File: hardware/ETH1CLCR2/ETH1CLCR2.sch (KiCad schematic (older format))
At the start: 0 parts

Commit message: PCB
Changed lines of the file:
@@
 F13 "TRIG_OUT" O R 8400 1600 50
 F14 "TRIG_IN" I R 8400 1700 50
-F15 "SPI2_MOSI" O L 6900 3750 50
-F16 "SPI2_NSS" O L 6900 3650 50
-F17 "SPI2_SCK" O L 6900 3850 50
-F18 "SPI1_NSS" O L 6900 4100 50
-F19 "SPI1_SCK" O L 6900 4200 50
-F20 "SPI1_MOSI" O L 6900 4300 50
-F21 "SPI3_MOSI" O L 6900 1900 50
-F22 "SPI3_MISO" I L 6900 2000 50
-F23 "SPI3_SCK" O L 6900 1800 50
-F24 "SPI3_NSS" O L 6900 1700 50
-F25 "CXN_REL5" O R 8400 3800 50
-F26 "CXN_REL4" O R 8400 3700 50
-F27 "CXN_REL3" O R 8400 3600 50
-F28 "CXN_REL2" O R 8400 3500 50
-F29 "CXN_REL1" O R 8400 3400 50
-F30 "IRR1" O L 6900 5900 50
-F31 "IRR2" O L 6900 6000 50
-F32 "IRR3" O L 6900 6100 50
-F33 "IRR4" O L 6900 6200 50
-F34 "IRR0" O L 6900 5800 50
-F35 "VDIFF2" O L 6900 5500 50
-F36 "VDIFF1" O L 6900 5400 50
-F37 "VDIFF0" O L 6900 5300 50
-F38 "IDIFF1" O L 6900 5700 50
-F39 "IDIFF0" O L 6900 5600 50
-F40 "SPI1_MISO" I L 6900 4000 50
-F41 "ADC1_RVS1" I L 6900 1500 50
-F42 "ADC1_RVS2" I L 6900 1600 50
+F15 "SPI2_NSS" O L 6900 2300 50
+F16 "SPI2_SCK" O L 6900 2400 50
+F17 "SPI1_NSS" O L 6900 4100 50
+F18 "SPI1_SCK" O L 6900 4200 50
+F19 "SPI1_MOSI" O L 6900 4300 50
+F20 "SPI3_MOSI" O L 6900 1900 50
+F21 "SPI3_MISO" I L 6900 2000 50
+F22 "SPI3_SCK" O L 6900 1800 50
+F23 "SPI3_NSS" O L 6900 1700 50
+F24 "CXN_REL5" O R 8400 3800 50
+F25 "CXN_REL4" O R 8400 3700 50
+F26 "CXN_REL3" O R 8400 3600 50
+F27 "CXN_REL2" O R 8400 3500 50
+F28 "CXN_REL1" O R 8400 3400 50
+F29 "IRR1" O L 6900 5900 50
+F30 "IRR2" O L 6900 6000 50
+F31 "IRR3" O L 6900 6100 50
+F32 "IRR4" O L 6900 6200 50
+F33 "IRR0" O L 6900 5800 50
+F34 "VDIFF2" O L 6900 5500 50
+F35 "VDIFF1" O L 6900 5400 50
+F36 "VDIFF0" O L 6900 5300 50
+F37 "IDIFF1" O L 6900 5700 50
+F38 "IDIFF0" O L 6900 5600 50
+F39 "SPI1_MISO" I L 6900 4000 50
+F40 "ADC1_RVS1" I L 6900 1500 50
+F41 "ADC1_RVS2" I L 6900 1600 50
+F42 "DDS_DIV2" O L 6900 4450 50
+F43 "DDS_DIV4" O L 6900 4550 50
+F44 "DDS_DIV8" O L 6900 4650 50
+F45 "~DDS_DIV10" O L 6900 4750 50
+F46 "SPI2_MISO" I L 6900 2500 50
+F47 "~ADC2_RST" O L 6900 2700 50
+F48 "ADC2_M0" O L 6900 2900 50
+F49 "ADC2_M1" O L 6900 2800 50
+F50 "ADC2_MDIV" O L 6900 2600 50
+F51 "~ADC2_HPF" O L 6900 3000 50
+F52 "SPI4_NSS" O L 6900 3650 50
+F53 "SPI4_MOSI" O L 6900 3750 50
+F54 "SPI4_SCK" O L 6900 3850 50
 $EndSheet
 Wire Wire Line
@@
 Wire Wire Line
 	6900 4300 6700 4300
+Wire Wire Line
+	6900 4450 6700 4450
+Wire Wire Line
+	6700 4550 6900 4550
+Wire Wire Line
+	6900 4650 6700 4650
+Wire Wire Line
+	6700 4750 6900 4750
+Wire Wire Line
+	6900 2500 6700 2500
+Wire Wire Line
+	6700 2400 6900 2400
+Wire Wire Line
+	6900 2300 6700 2300
+Wire Wire Line
+	6900 2700 6700 2700
+Wire Wire Line
+	6900 2900 6700 2900
+Wire Wire Line
+	6900 2800 6700 2800
+Wire Wire Line
+	6900 3000 6700 3000
+Wire Wire Line
+	6700 2600 6900 2600
 $EndSCHEMATC

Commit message: PCB
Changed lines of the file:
@@
 F15 "SPI2_NSS" O L 6900 2300 50
 F16 "SPI2_SCK" O L 6900 2400 50
-F17 "SPI1_NSS" O L 6900 4100 50
-F18 "SPI1_SCK" O L 6900 4200 50
-F19 "SPI1_MOSI" O L 6900 4300 50
-F20 "SPI3_MOSI" O L 6900 1900 50
-F21 "SPI3_MISO" I L 6900 2000 50
-F22 "SPI3_SCK" O L 6900 1800 50
-F23 "SPI3_NSS" O L 6900 1700 50
-F24 "CXN_REL5" O R 8400 3800 50
-F25 "CXN_REL4" O R 8400 3700 50
-F26 "CXN_REL3" O R 8400 3600 50
-F27 "CXN_REL2" O R 8400 3500 50
-F28 "CXN_REL1" O R 8400 3400 50
-F29 "IRR1" O L 6900 5900 50
-F30 "IRR2" O L 6900 6000 50
-F31 "IRR3" O L 6900 6100 50
-F32 "IRR4" O L 6900 6200 50
-F33 "IRR0" O L 6900 5800 50
-F34 "VDIFF2" O L 6900 5500 50
-F35 "VDIFF1" O L 6900 5400 50
-F36 "VDIFF0" O L 6900 5300 50
-F37 "IDIFF1" O L 6900 5700 50
-F38 "IDIFF0" O L 6900 5600 50
-F39 "SPI1_MISO" I L 6900 4000 50
-F40 "ADC1_RVS1" I L 6900 1500 50
-F41 "ADC1_RVS2" I L 6900 1600 50
-F42 "DDS_DIV2" O L 6900 4450 50
-F43 "DDS_DIV4" O L 6900 4550 50
-F44 "DDS_DIV8" O L 6900 4650 50
-F45 "~DDS_DIV10" O L 6900 4750 50
-F46 "SPI2_MISO" I L 6900 2500 50
-F47 "~ADC2_RST" O L 6900 2700 50
-F48 "ADC2_M0" O L 6900 2900 50
-F49 "ADC2_M1" O L 6900 2800 50
-F50 "ADC2_MDIV" O L 6900 2600 50
-F51 "~ADC2_HPF" O L 6900 3000 50
-F52 "SPI4_NSS" O L 6900 3650 50
-F53 "SPI4_MOSI" O L 6900 3750 50
-F54 "SPI4_SCK" O L 6900 3850 50
+F17 "SPI3_MOSI" O L 6900 1900 50
+F18 "SPI3_MISO" I L 6900 2000 50
+F19 "SPI3_SCK" O L 6900 1800 50
+F20 "SPI3_NSS" O L 6900 1700 50
+F21 "CXN_REL5" O R 8400 3800 50
+F22 "CXN_REL4" O R 8400 3700 50
+F23 "CXN_REL3" O R 8400 3600 50
+F24 "CXN_REL2" O R 8400 3500 50
+F25 "CXN_REL1" O R 8400 3400 50
+F26 "IRR1" O L 6900 5900 50
+F27 "IRR2" O L 6900 6000 50
+F28 "IRR3" O L 6900 6100 50
+F29 "IRR4" O L 6900 6200 50
+F30 "IRR0" O L 6900 5800 50
+F31 "VDIFF2" O L 6900 5500 50
+F32 "VDIFF1" O L 6900 5400 50
+F33 "VDIFF0" O L 6900 5300 50
+F34 "IDIFF1" O L 6900 5700 50
+F35 "IDIFF0" O L 6900 5600 50
+F36 "ADC1_RVS1" I L 6900 1500 50
+F37 "ADC1_RVS2" I L 6900 1600 50
+F38 "DDS_DIV2" O L 6900 4450 50
+F39 "DDS_DIV4" O L 6900 4550 50
+F40 "DDS_DIV8" O L 6900 4650 50
+F41 "~DDS_DIV10" O L 6900 4750 50
+F42 "SPI2_MISO" I L 6900 2500 50
+F43 "~ADC2_RST" O L 6900 2700 50
+F44 "ADC2_M0" O L 6900 2900 50
+F45 "ADC2_M1" O L 6900 2800 50
+F46 "ADC2_MDIV" O L 6900 2600 50
+F47 "~ADC2_HPF" O L 6900 3000 50
+F48 "SPI4_NSS" O L 6900 3650 50
+F49 "SPI4_MOSI" O L 6900 3750 50
+F50 "SPI4_SCK" O L 6900 3850 50
+F51 "SPI5_MOSI" O L 6900 4300 50
+F52 "SPI5_MISO" I L 6900 4000 50
+F53 "SPI5_SCK" O L 6900 4200 50
+F54 "SPI5_NSS" O L 6900 4100 50
 $EndSheet
 Wire Wire Line

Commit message: PCB
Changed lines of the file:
@@
 	3950 5700 6900 5700
 Wire Wire Line
-	5000 3750 4450 3750
-Wire Wire Line
-	4450 3750 4450 1200
+	5000 3550 4450 3550
+Wire Wire Line
+	4450 3550 4450 1200
 Wire Wire Line
 	4450 1200 9900 1200
@@
 F36 "ADC1_RVS1" I L 6900 1500 50
 F37 "ADC1_RVS2" I L 6900 1600 50
-F38 "DDS_DIV2" O L 6900 4450 50
-F39 "DDS_DIV4" O L 6900 4550 50
-F40 "DDS_DIV8" O L 6900 4650 50
-F41 "~DDS_DIV10" O L 6900 4750 50
+F38 "DDS_DIV2" O L 6900 4250 50
+F39 "DDS_DIV4" O L 6900 4350 50
+F40 "DDS_DIV8" O L 6900 4450 50
+F41 "~DDS_DIV10" O L 6900 4550 50
 F42 "SPI2_MISO" I L 6900 2500 50
 F43 "~ADC2_RST" O L 6900 2700 50
@@
 F46 "ADC2_MDIV" O L 6900 2600 50
 F47 "~ADC2_HPF" O L 6900 3000 50
-F48 "SPI4_NSS" O L 6900 3650 50
-F49 "SPI4_MOSI" O L 6900 3750 50
-F50 "SPI4_SCK" O L 6900 3850 50
-F51 "SPI5_MOSI" O L 6900 4300 50
-F52 "SPI5_MISO" I L 6900 4000 50
-F53 "SPI5_SCK" O L 6900 4200 50
-F54 "SPI5_NSS" O L 6900 4100 50
+F48 "SPI4_NSS" O L 6900 3450 50
+F49 "SPI4_MOSI" O L 6900 3550 50
+F50 "SPI4_SCK" O L 6900 3650 50
+F51 "SPI5_MOSI" O L 6900 4100 50
+F52 "SPI5_MISO" I L 6900 3800 50
+F53 "SPI5_SCK" O L 6900 4000 50
+F54 "SPI5_NSS" O L 6900 3900 50
+F55 "ADC_SEL" O L 6900 2150 50
+F56 "MUX_A0" O L 6900 4650 50
+F57 "MUX_A1" O L 6900 4750 50
+F58 "DDS_LPF" O L 6900 4850 50
 $EndSheet
 Wire Wire Line
@@
 	6700 1600 6900 1600
 $Sheet
-S 5000 3550 1700 1450
+S 5000 3350 1700 1600
 U 610F1C70
 F0 "DDS" 50
 F1 "DDS.sch" 50
-F2 "H_CUR" O L 5000 3750 50
-F3 "DDS_SCLK" I R 6700 3850 50
-F4 "DDS_SDATA" I R 6700 3750 50
-F5 "DDS_CS" I R 6700 3650 50
-F6 "MDAC_SDO" O R 6700 4000 50
-F7 "MDAC_CS" I R 6700 4100 50
-F8 "MDAC_SCK" I R 6700 4200 50
-F9 "MDAC_SDIN" I R 6700 4300 50
-F10 "DDS_DIV2" I R 6700 4450 50
-F11 "DDS_DIV4" I R 6700 4550 50
-F12 "DDS_DIV8" I R 6700 4650 50
-F13 "~DDS_DIV10" I R 6700 4750 50
-F14 "DDS_CLK" O L 5000 3950 50
+F2 "H_CUR" O L 5000 3550 50
+F3 "DDS_SCLK" I R 6700 3650 50
+F4 "DDS_SDATA" I R 6700 3550 50
+F5 "DDS_CS" I R 6700 3450 50
+F6 "MDAC_SDO" O R 6700 3800 50
+F7 "MDAC_CS" I R 6700 3900 50
+F8 "MDAC_SCK" I R 6700 4000 50
+F9 "MDAC_SDIN" I R 6700 4100 50
+F10 "DDS_DIV2" I R 6700 4250 50
+F11 "DDS_DIV4" I R 6700 4350 50
+F12 "DDS_DIV8" I R 6700 4450 50
+F13 "~DDS_DIV10" I R 6700 4550 50
+F14 "DDS_CLK" O L 5000 3750 50
+F15 "MUX_A0" I R 6700 4650 50
+F16 "MUX_A1" I R 6700 4750 50
+F17 "DDS_LPF" I R 6700 4850 50
 $EndSheet
 Wire Wire Line
-	5000 3950 4650 3950
-Wire Wire Line
-	4650 3950 4650 1900
+	5000 3750 4650 3750
+Wire Wire Line
+	4650 3750 4650 1900
 Wire Wire Line
 	4650 1900 5000 1900
 Wire Wire Line
+	6900 3450 6700 3450
+Wire Wire Line
+	6700 3550 6900 3550
+Wire Wire Line
 	6900 3650 6700 3650
 Wire Wire Line
-	6700 3750 6900 3750
-Wire Wire Line
-	6900 3850 6700 3850
+	6700 3800 6900 3800
+Wire Wire Line
+	6900 3900 6700 3900
 Wire Wire Line
 	6700 4000 6900 4000
@@
 	6900 4100 6700 4100
 Wire Wire Line
-	6700 4200 6900 4200
-Wire Wire Line
-	6900 4300 6700 4300
+	6900 4250 6700 4250
+Wire Wire Line
+	6700 4350 6900 4350
 Wire Wire Line
 	6900 4450 6700 4450
@@
 	6700 4550 6900 4550
 Wire Wire Line
-	6900 4650 6700 4650
+	6900 2500 6700 2500
+Wire Wire Line
+	6700 2400 6900 2400
+Wire Wire Line
+	6900 2300 6700 2300
+Wire Wire Line
+	6900 2700 6700 2700
+Wire Wire Line
+	6900 2900 6700 2900
+Wire Wire Line
+	6900 2800 6700 2800
+Wire Wire Line
+	6900 3000 6700 3000
+Wire Wire Line
+	6700 2600 6900 2600
+Wire Wire Line
+	6900 2150 6700 2150
+Wire Wire Line
+	6900 4850 6700 4850
 Wire Wire Line
 	6700 4750 6900 4750
 Wire Wire Line
-	6900 2500 6700 2500
-Wire Wire Line
-	6700 2400 6900 2400
-Wire Wire Line
-	6900 2300 6700 2300
-Wire Wire Line
-	6900 2700 6700 2700
-Wire Wire Line
-	6900 2900 6700 2900
-Wire Wire Line
-	6900 2800 6700 2800
-Wire Wire Line
-	6900 3000 6700 3000
-Wire Wire Line
-	6700 2600 6900 2600
+	6700 4650 6900 4650
 $EndSCHEMATC

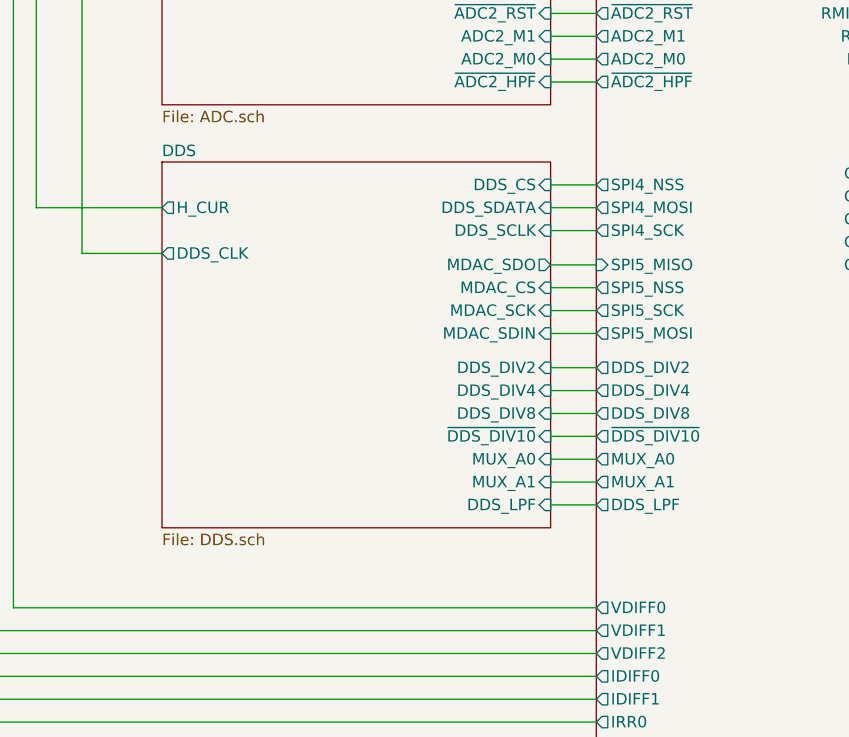
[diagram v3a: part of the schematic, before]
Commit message: Modification in schematic and PCB
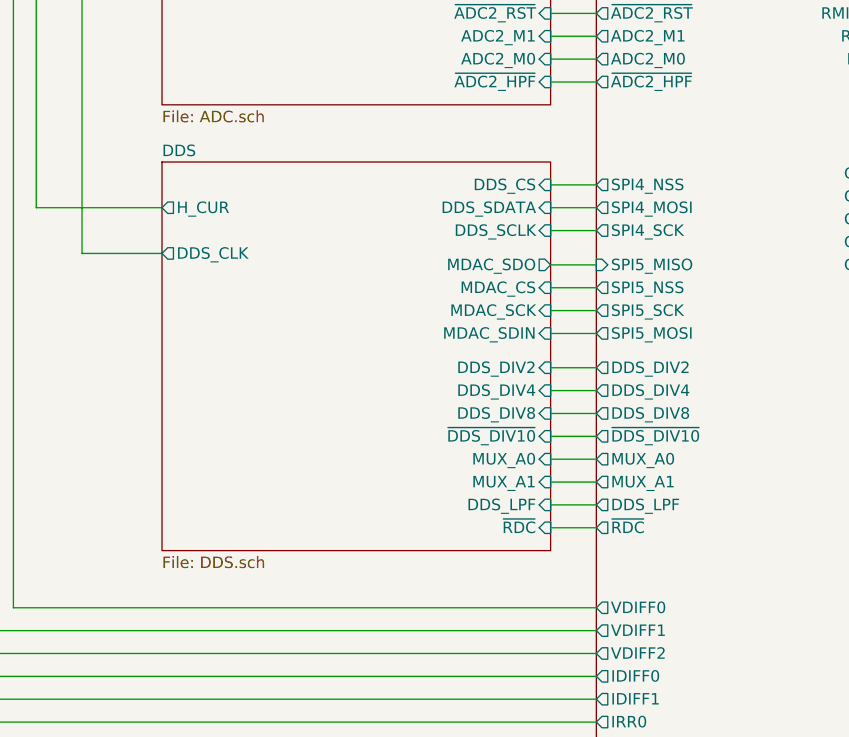
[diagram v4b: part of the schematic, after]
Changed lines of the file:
@@
 F57 "MUX_A1" O L 6900 4750 50
 F58 "DDS_LPF" O L 6900 4850 50
+F59 "~RDC" O L 6900 4950 50
 $EndSheet
 Wire Wire Line
@@
 	6700 1600 6900 1600
 $Sheet
-S 5000 3350 1700 1600
+S 5000 3350 1700 1700
 U 610F1C70
 F0 "DDS" 50
@@
 F16 "MUX_A1" I R 6700 4750 50
 F17 "DDS_LPF" I R 6700 4850 50
+F18 "~RDC" I R 6700 4950 50
 $EndSheet
 Wire Wire Line
@@
 Wire Wire Line
 	6700 4650 6900 4650
+Wire Wire Line
+	6900 4950 6700 4950
 $EndSCHEMATC

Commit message: PCB done
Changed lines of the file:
@@
 $EndSheet
 $Sheet
-S 9900 800  750  3100
+S 9900 800  750  3200
 U 60A4F32B
 F0 "Connector" 50
@@
 F14 "H_POT" I L 9900 1100 50
 F15 "L_POT" I L 9900 1000 50
+F16 "CXN_REL6" I L 9900 3900 50
 $EndSheet
 Wire Wire Line
@@
 F58 "DDS_LPF" O L 6900 4850 50
 F59 "~RDC" O L 6900 4950 50
+F60 "CXN_REL6" O R 8400 3900 50
 $EndSheet
 Wire Wire Line
@@
 Wire Wire Line
 	6900 4950 6700 4950
+Wire Wire Line
+	9900 3900 8400 3900
 $EndSCHEMATC
